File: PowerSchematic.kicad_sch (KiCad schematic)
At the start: 10 parts, among them J1 USB_C_Receptacle_PowerOnly_6P, Q1 Q_Dual_NMOS_S1G1S2G2D2D1, U1 TP4056-42-ESOP8, U2 DW01A, U3 LGS5500EP

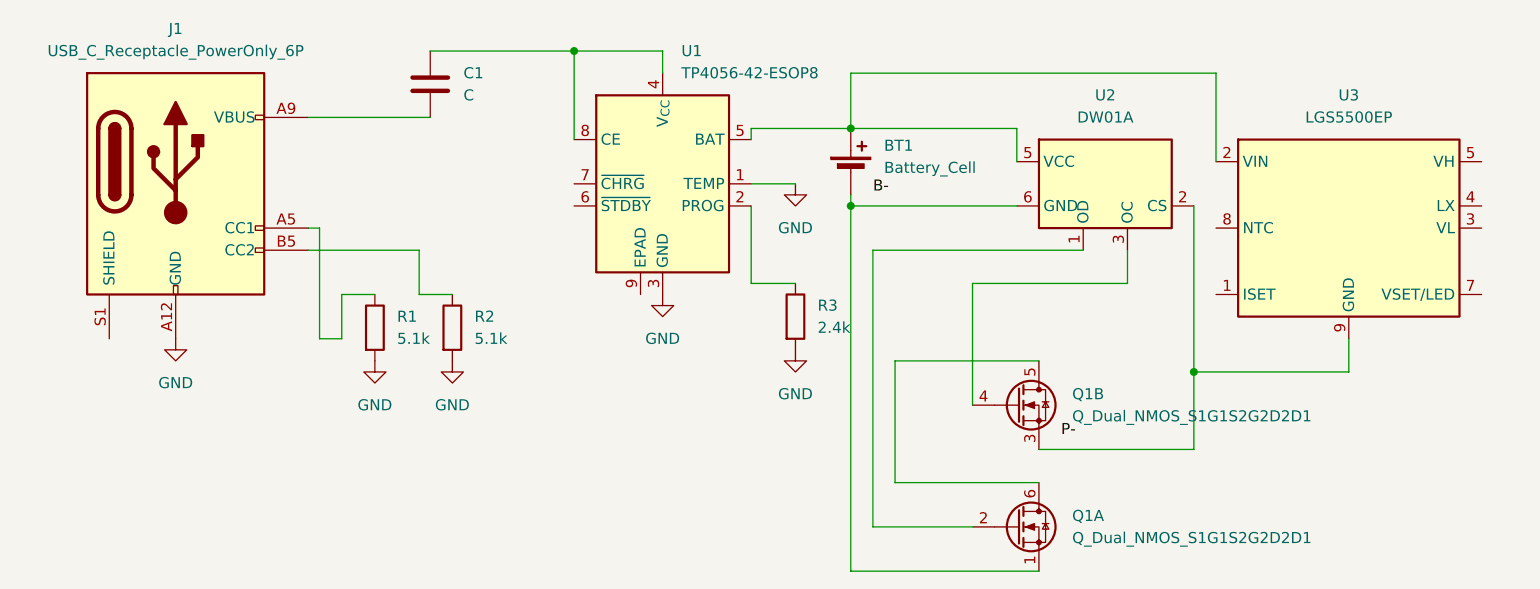
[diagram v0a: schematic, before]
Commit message: New power schematic
Here is the updated power schematic with the LiPo battery changes flavin suggested
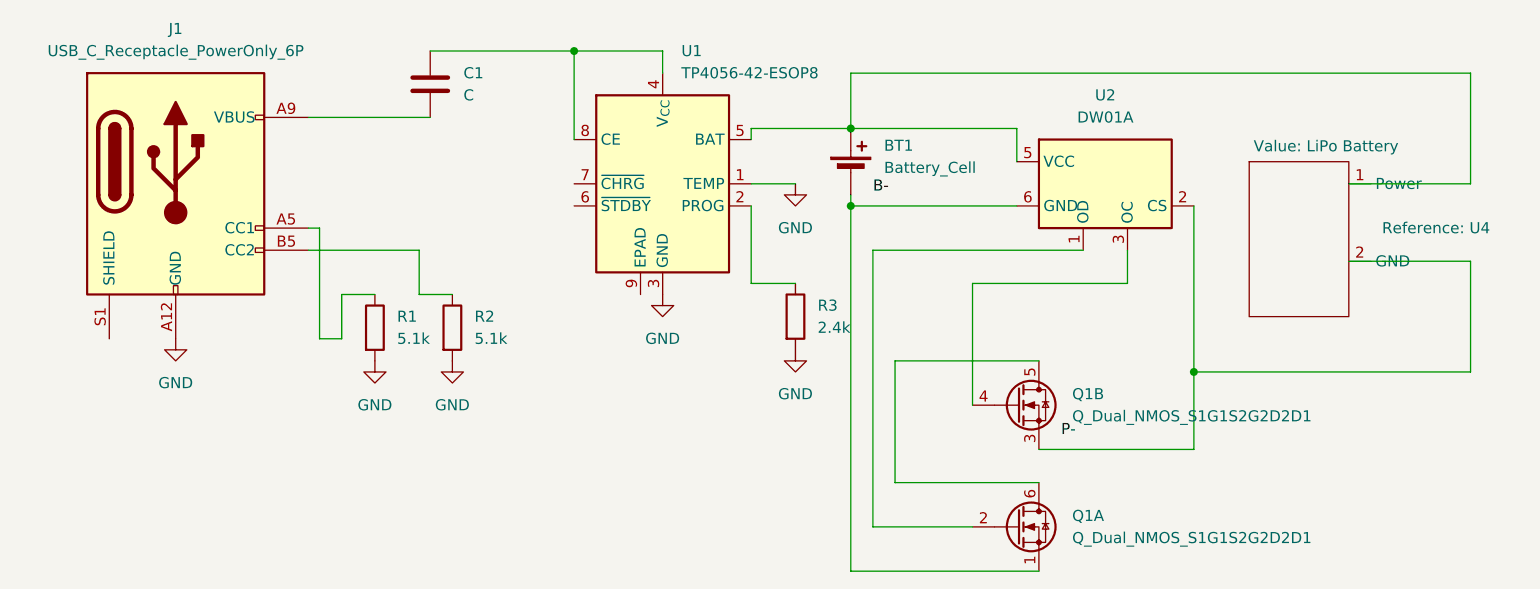
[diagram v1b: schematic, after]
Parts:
- removed U3: LGS5500EP, Package_SO:SOIC-8-1EP_3.9x4.9mm_P1.27mm_EP2.41x3.3mm, symbol Battery_Management:LGS5500EP
- added U4: LiPo Battery, symbol sensors:Battery
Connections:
- net at Q1.3 (S), U2.2 (CS): now also U4.2 (GND)
- net at BT1.1 (+), U1.5 (BAT), U2.5 (VCC): now also U4.1 (Power)
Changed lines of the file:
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@@
+	(wire
+		(pts
+			(xy 186.69 104.14) (xy 186.69 91.44)
+		)
+		(stroke
+			(width 0)
+			(type default)
+		)
+	)
 	(wire
 		(pts
@@
 	(wire
 		(pts
+			(xy 186.69 82.55) (xy 186.69 69.85)
+		)
+		(stroke
+			(width 0)
+			(type default)
+		)
+	)
+	(wire
+		(pts
 			(xy 134.62 76.2) (xy 115.57 76.2)
 		)
@@
 	(wire
 		(pts
-			(xy 172.72 104.14) (xy 154.94 104.14)
+			(xy 154.94 104.14) (xy 186.69 104.14)
 		)
 		(stroke
@@
 	(wire
 		(pts
-			(xy 157.48 80.01) (xy 157.48 69.85)
-		)
-		(stroke
-			(width 0)
-			(type default)
-		)
-	)
-	(wire
-		(pts
 			(xy 104.14 76.2) (xy 104.14 77.47)
 		)
@@
 	(wire
 		(pts
-			(xy 172.72 100.33) (xy 172.72 104.14)
-		)
-		(stroke
-			(width 0)
-			(type default)
-		)
-	)
-	(wire
-		(pts
 			(xy 54.61 100.33) (xy 54.61 87.63)
 		)
@@
 	(wire
 		(pts
-			(xy 157.48 69.85) (xy 115.57 69.85)
+			(xy 115.57 69.85) (xy 186.69 69.85)
 		)
 		(stroke
@@
 		(pts
 			(xy 53.34 74.93) (xy 67.31 74.93)
+		)
+		(stroke
+			(width 0)
+			(type default)
+		)
+	)
+	(wire
+		(pts
+			(xy 172.72 82.55) (xy 186.69 82.55)
+		)
+		(stroke
+			(width 0)
+			(type default)
+		)
+	)
+	(wire
+		(pts
+			(xy 186.69 91.44) (xy 172.72 91.44)
 		)
 		(stroke
@@
 	)
 	(symbol
-		(lib_id "Battery_Management:LGS5500EP")
-		(at 172.72 87.63 0)
-		(unit 1)
-		(exclude_from_sim no)
-		(in_bom yes)
-		(on_board yes)
-		(dnp no)
-		(fields_autoplaced yes)
-		(property "Reference" "U3"
-			(at 172.72 72.39 0)
-			(effects
-				(font
-					(size 1.27 1.27)
-				)
-			)
-		)
-		(property "Value" "LGS5500EP"
-			(at 172.72 74.93 0)
-			(effects
-				(font
-					(size 1.27 1.27)
-				)
-			)
-		)
-		(property "Footprint" "Package_SO:SOIC-8-1EP_3.9x4.9mm_P1.27mm_EP2.41x3.3mm"
-			(at 172.466 117.602 0)
-			(effects
-				(font
-					(size 1.27 1.27)
-				)
-				(hide yes)
-			)
-		)
-		(property "Datasheet" "https://www.lcsc.com/datasheet/lcsc_datasheet_2304071430_Legend-Si-LGS5500EP_C5280699.pdf"
-			(at 172.974 113.284 0)
-			(effects
-				(font
-					(size 1.27 1.27)
-				)
-				(hide yes)
-			)
-		)
-		(property "Description" "LiPo charger and 5V boost converter, 4.5-5.5V input, 4.2-4.4V battery, 400-1000mA charge current, 800mA boost output, SOIC-8-1EP"
-			(at 172.72 115.57 0)
-			(effects
-				(font
-					(size 1.27 1.27)
-				)
-				(hide yes)
-			)
-		)
-		(pin "2"
-		)
-		(pin "8"
-		)
-		(pin "1"
-		)
-		(pin "6"
-		)
-		(pin "9"
-		)
-		(pin "5"
-		)
-		(pin "4"
-		)
-		(pin "3"
-		)
-		(pin "7"
-		)
-		(instances
-			(project ""
-				(path "/6da40207-23a9-469e-b250-03966f5b936e"
-					(reference "U3")
-					(unit 1)
-				)
-			)
-		)
-	)
-	(symbol
 		(lib_id "power:GND")
 		(at 60.96 102.87 0)
@@
 					(unit 1)
 				)
+			)
+		)
+	)
+	(symbol
+		(lib_id "sensors:Battery")
+		(at 167.64 77.47 0)
+		(unit 1)
+		(exclude_from_sim no)
+		(in_bom yes)
+		(on_board yes)
+		(dnp no)
+		(property "Reference" "U4"
+			(at 176.53 87.6299 0)
+			(show_name yes)
+			(effects
+				(font
+					(size 1.27 1.27)
+				)
+				(justify left)
+			)
+		)
+		(property "Value" "LiPo Battery"
+			(at 161.798 78.232 0)
+			(show_name yes)
+			(effects
+				(font
+					(size 1.27 1.27)
+				)
+				(justify left)
+			)
+		)
+		(property "Footprint" ""
+			(at 167.64 77.47 0)
+			(effects
+				(font
+					(size 1.27 1.27)
+				)
+				(hide yes)
+			)
+		)
+		(property "Datasheet" ""
+			(at 167.64 77.47 0)
+			(effects
+				(font
+					(size 1.27 1.27)
+				)
+				(hide yes)
+			)
+		)
+		(property "Description" ""
+			(at 167.64 77.47 0)
+			(effects
+				(font
+					(size 1.27 1.27)
+				)
+				(hide yes)
+			)
+		)
+		(pin "1"
+		)
+		(pin "2"
+		)
+		(instances
+			(project ""
+				(path "/6da40207-23a9-469e-b250-03966f5b936e"
+					(reference "U4")
+					(unit 1)
+				)
